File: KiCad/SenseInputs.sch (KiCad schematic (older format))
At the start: 39 parts, among them U401 ADS1115IDGST, U402 ADS1115IDGST, U403 X95840

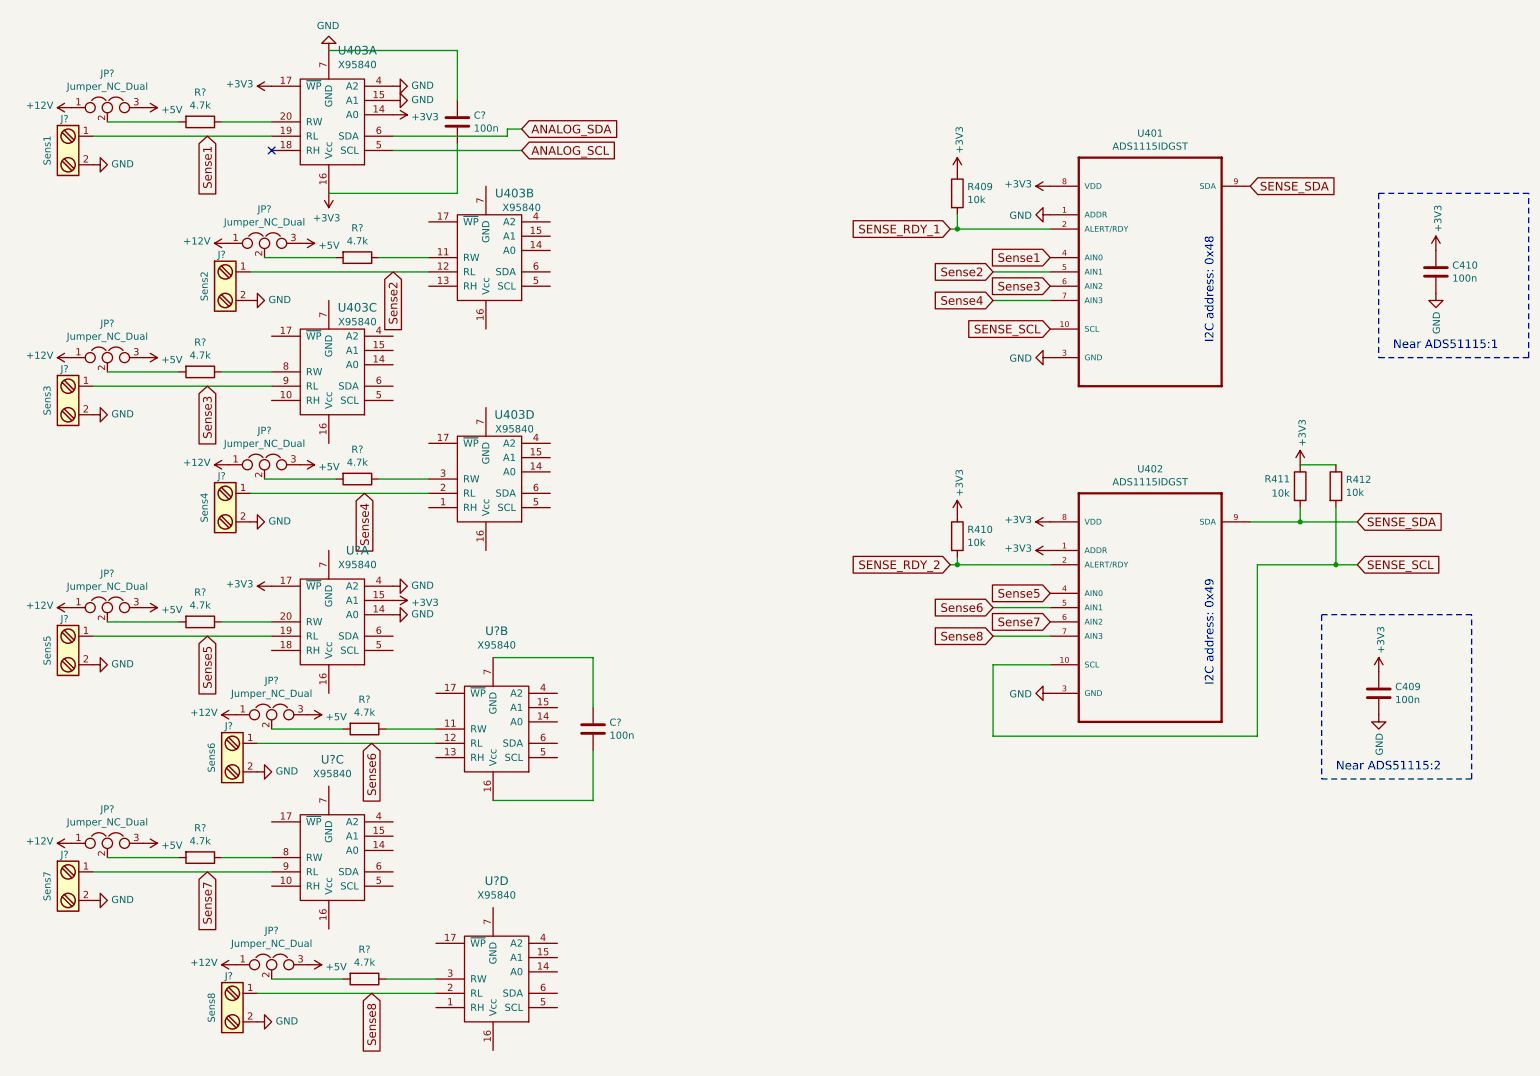
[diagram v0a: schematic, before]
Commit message: Save with sensor inputs using digital potentiometer
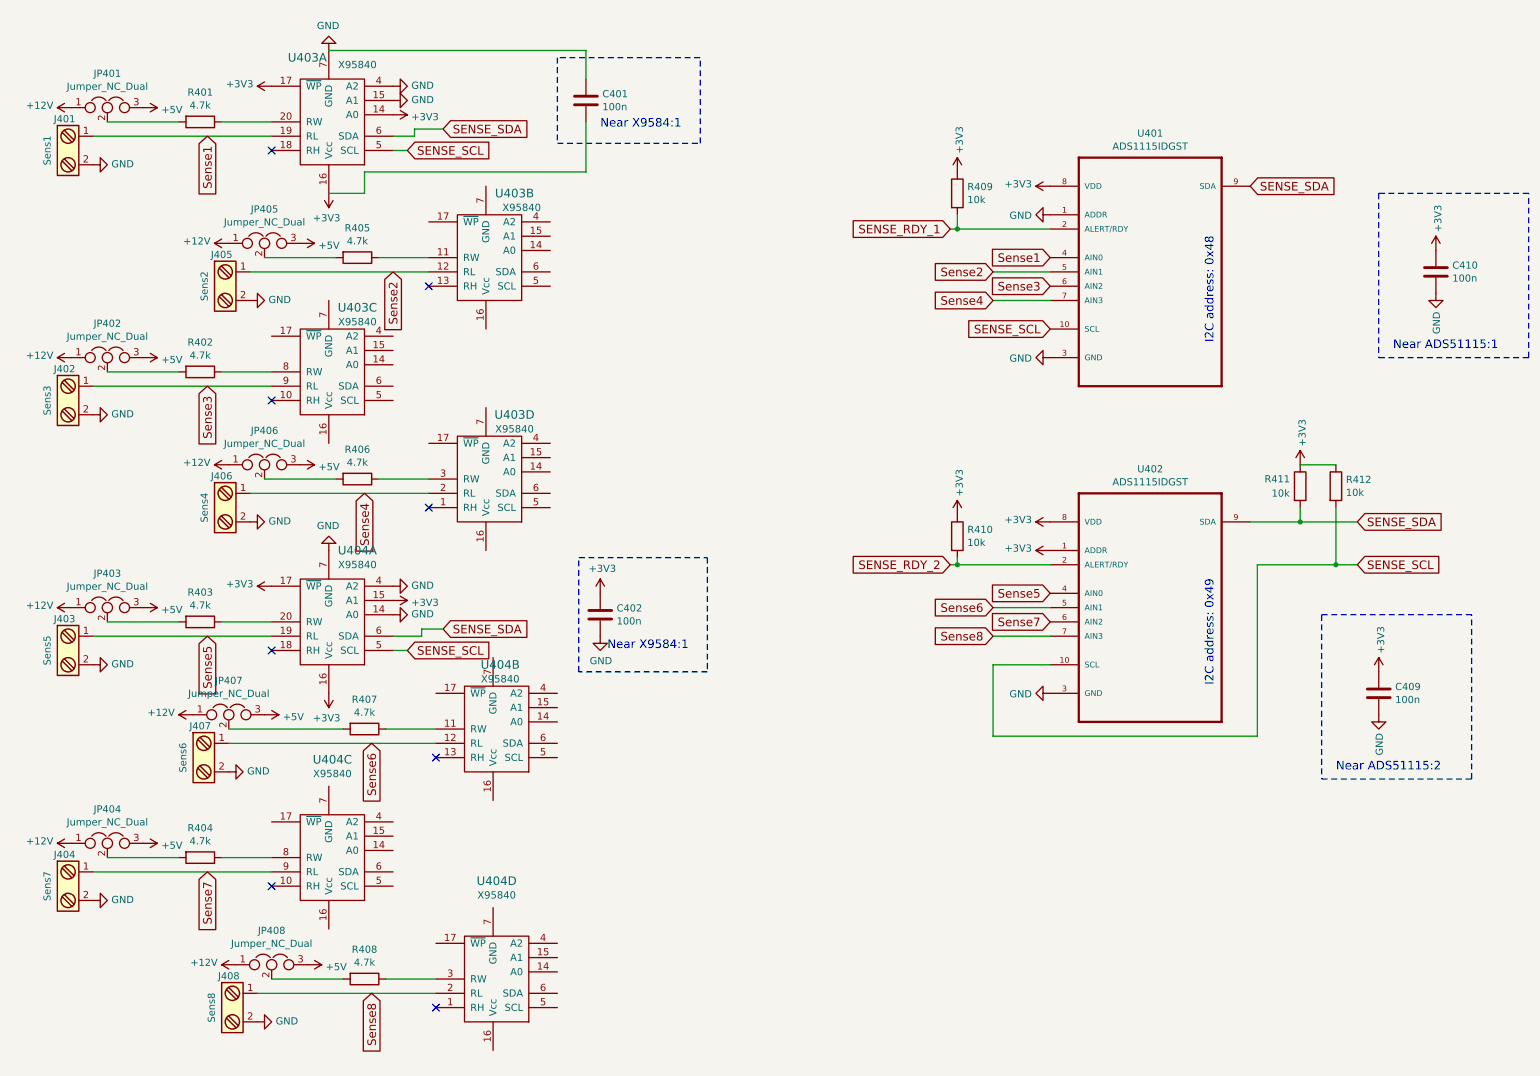
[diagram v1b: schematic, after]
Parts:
- removed R? (x7): 4.7k, symbol R
- added R401, R402, R403, R404, R405, R406, R407: 4.7k, Resistors_SMD:R_0805, symbol R
- R408: renamed from R?; footprint (none) -> Resistors_SMD:R_0805
- gave numbers to parts that had none: 19
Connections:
- net ANALOG_SCL is gone; now on net SENSE_SCL: U403.5 (SCL)
- net ANALOG_SDA is gone; now on net SENSE_SDA: U403.6 (SDA)
- net +3V3: now also C402.1, U404.16 (Vcc)
- net GND: now also C402.2, U404.7 (GND)
- net SENSE_SCL: now also U404.5 (SCL)
- net SENSE_SDA: now also U404.6 (SDA)
- net at U403.20 (RW): now also R401.1
- net at U403.11 (RW): now also R405.1
- net at U403.8 (RW): now also R402.1
- net at U403.3 (RW): now also R406.1
- net at JP401.2: now also R401.2
- net at U404.20 (RW): now also R403.1
- net at U404.11 (RW): now also R407.1
- net at U404.16 (Vcc): no longer C402.2
- net at U404.7 (GND): no longer C402.1
- net at U404.8 (RW): now also R404.1
- net at JP405.2: now also R405.2
- net at JP402.2: now also R402.2
- net at JP406.2: now also R406.2
- net at JP403.2: now also R403.2
- net at JP407.2: now also R407.2
- net at JP404.2: now also R404.2
- no-connect marks 1 -> 8
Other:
- note added: "Near X9584:1"
- moved on the sheet: C401, C402, J407, JP407

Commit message: Inputs reworked. New terminals
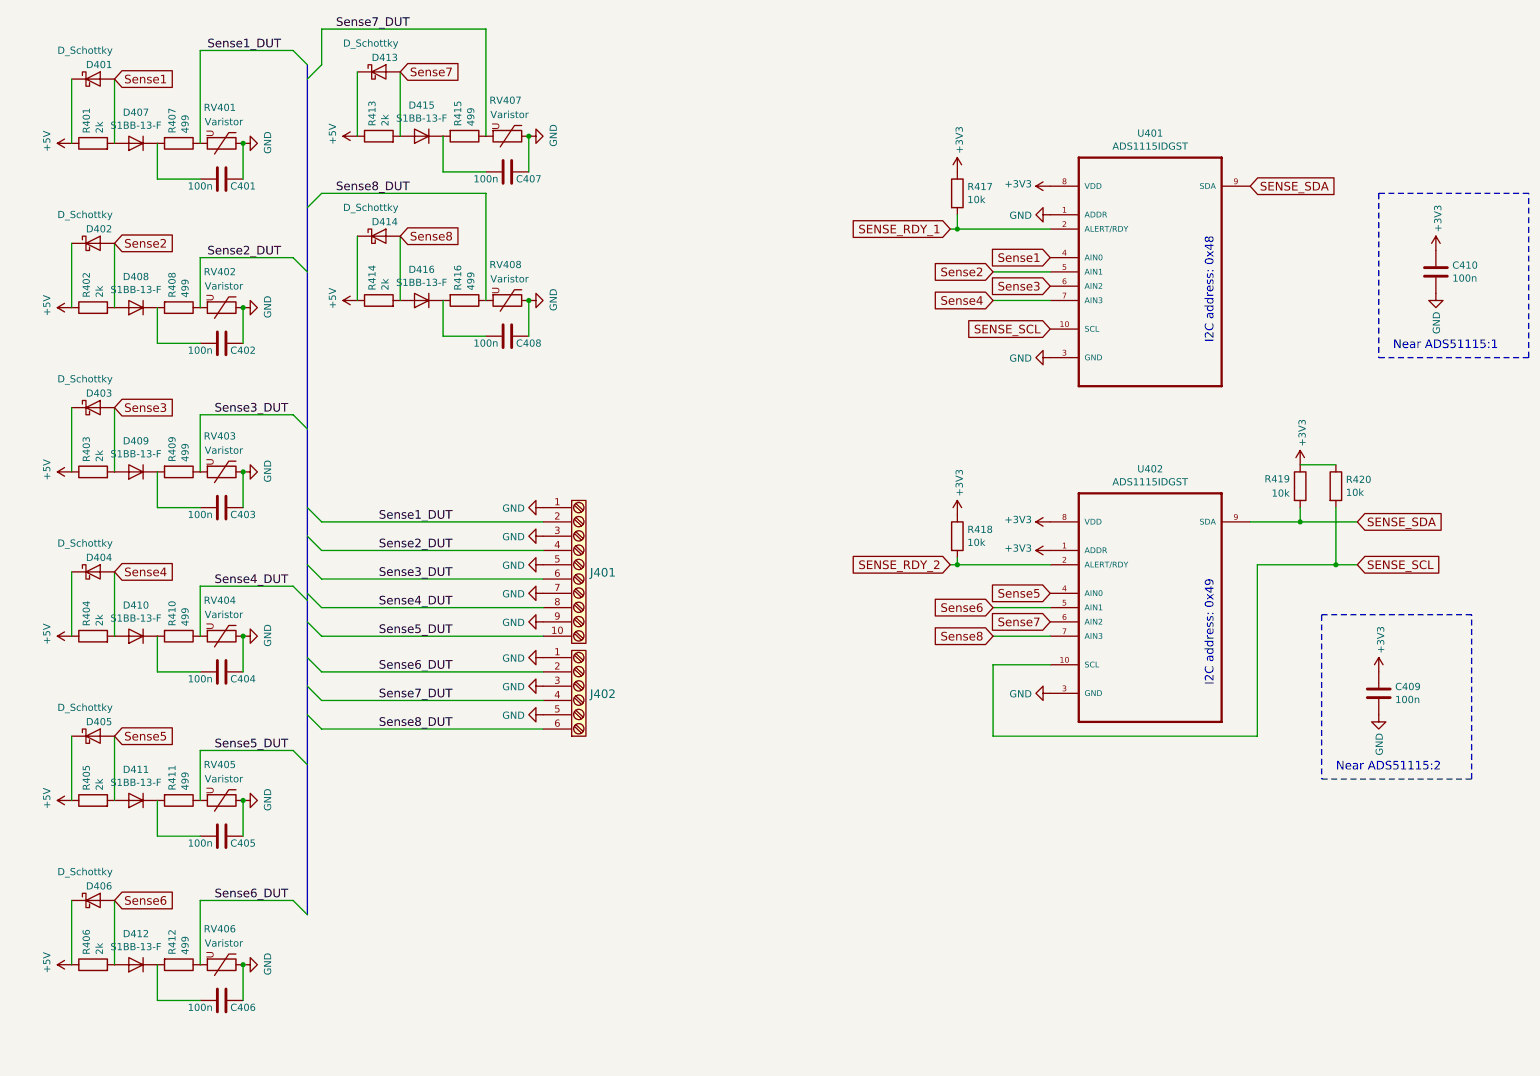
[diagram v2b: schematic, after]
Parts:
- removed J401: Sens1, Connectors_Terminal_Blocks:TerminalBlock_Pheonix_MPT-2.54mm_2pol, symbol Screw_Terminal_1x02
- removed J402: Sens3, Connectors_Terminal_Blocks:TerminalBlock_Pheonix_MPT-2.54mm_2pol, symbol Screw_Terminal_1x02
- removed J403: Sens5, Connectors_Terminal_Blocks:TerminalBlock_Pheonix_MPT-2.54mm_2pol, symbol Screw_Terminal_1x02
- removed J404: Sens7, Connectors_Terminal_Blocks:TerminalBlock_Pheonix_MPT-2.54mm_2pol, symbol Screw_Terminal_1x02
- removed J405: Sens2, Connectors_Terminal_Blocks:TerminalBlock_Pheonix_MPT-2.54mm_2pol, symbol Screw_Terminal_1x02
- removed J406: Sens4, Connectors_Terminal_Blocks:TerminalBlock_Pheonix_MPT-2.54mm_2pol, symbol Screw_Terminal_1x02
- removed J407: Sens6, Connectors_Terminal_Blocks:TerminalBlock_Pheonix_MPT-2.54mm_2pol, symbol Screw_Terminal_1x02
- removed J408: Sens8, Connectors_Terminal_Blocks:TerminalBlock_Pheonix_MPT-2.54mm_2pol, symbol Screw_Terminal_1x02
- removed JP401, JP402, JP403, JP404, JP405, JP406, JP407, JP408: Jumper_NC_Dual, symbol Jumper_NC_Dual
- removed U403, U404: X95840, symbol X95840
- added C403, C404, C405, C406, C407, C408: 100n, Capacitors_SMD:C_0805, symbol C
- added D401, D402, D403, D404, D405, D406, D413, D414: D_Schottky, Diodes_SMD:D_SOD-123, symbol D_Schottky
- added D407, D408, D409, D410, D411, D412, D415, D416: S1BB-13-F, Diodes_SMD:D_SMB, symbol 1N4007
- added J401: TE_Connectivity_1-282834-0, TE_Connectivity:TE_Connectivity_1-282834-0, symbol TE_Connectivity_1-282834-0
- added J402: TE_Connectivity_282834-6, TE_Connectivity:TE_Connectivity_282834-6, symbol TE_Connectivity_282834-6
- added R409, R410, R411, R412, R415, R416: 499, Resistors_SMD:R_0805, symbol R
- added R413, R414: 2k, Resistors_SMD:R_0805, symbol R
- added RV401, RV402, RV403, RV404, RV405, RV406, RV407, RV408: Varistor, Resistors_SMD:R_0805, symbol Varistor
- R401, R402, R403, R404, R405, R406: value 4.7k -> 2k
- R407, R408: value 4.7k -> 499
- renumbered R409 to R417, R410 to R418, R411 to R419, R412 to R420
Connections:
- net +3V3: no longer C401.2, C402.1
- net +5V: now also R401.1, R402.1, R403.1, R404.1, R405.1, R406.1, D401.1 (K), D402.1 (K), D403.1 (K), D404.1 (K), D405.1 (K), D406.1 (K), D413.1 (K), D414.1 (K), R413.1, R414.1
- net GND: now also C401.2, C403.2, C404.2, C405.2, C406.2, C407.2, C408.2, J401.1, J401.3, J401.5, J401.7, J401.9, J402.1, J402.3, J402.5, RV401.1, RV402.1, RV403.1, RV404.1, RV405.1, RV406.1, RV407.1, RV408.1; no longer C401.1
- net Sense1: now also R401.2, D401.2 (A), D407.2 (A)
- net Sense2: now also R402.2, D402.2 (A), D408.2 (A)
- net Sense3: now also R403.2, D403.2 (A), D409.2 (A)
- net Sense4: now also R404.2, D404.2 (A), D410.2 (A)
- net Sense5: now also R405.2, D405.2 (A), D411.2 (A)
- net Sense6: now also R406.2, D406.2 (A), D412.2 (A)
- net Sense7: now also D413.2 (A), D415.2 (A), R413.2
- net Sense8: now also D414.2 (A), D416.2 (A), R414.2
- net Sense1_DUT: now reaches R407.1
- net Sense1_DUT: now also J401.2, RV401.2
- net Sense2_DUT: now reaches R408.1
- net Sense2_DUT: now also J401.4, RV402.2
- net at R407.2: now also C401.1, D407.1 (K)
- net at R408.2: now also C402.1, D408.1 (K)
- new net: C403.1, D409.1 (K), R409.2
- new net: C404.1, D410.1 (K), R410.2
- new net: C405.1, D411.1 (K), R411.2
- new net: C406.1, D412.1 (K), R412.2
- new net: C407.1, D415.1 (K), R415.2
- new net: C408.1, D416.1 (K), R416.2
- new net Sense3_DUT: J401.6, R409.1, RV403.2
- new net Sense4_DUT: J401.8, R410.1, RV404.2
- new net Sense5_DUT: J401.10, R411.1, RV405.2
- new net Sense6_DUT: J402.2, R412.1, RV406.2
- new net Sense7_DUT: J402.4, R415.1, RV407.2
- new net Sense8_DUT: J402.6, R416.1, RV408.2
- no-connect marks 8 -> 0
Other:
- note removed: "Near X9584:1"
